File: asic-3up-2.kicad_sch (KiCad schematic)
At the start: 79 parts, among them J16 Conn_01x01, J17 Conn_01x01, J8 Conn_01x01, J9 Conn_01x01, U57 MCP1824T-1202E/OT, U58 MCP1824T-1202E/OT, U59 MCP1824T-1202E/OT, U60 MCP1824T-0802E, U61 MCP1824T-0802E, U62 MCP1824T-0802E, U63 BM1362AC_MODE1, U64 BM1362AC_MODE0, U65 BM1362AC_MODE1

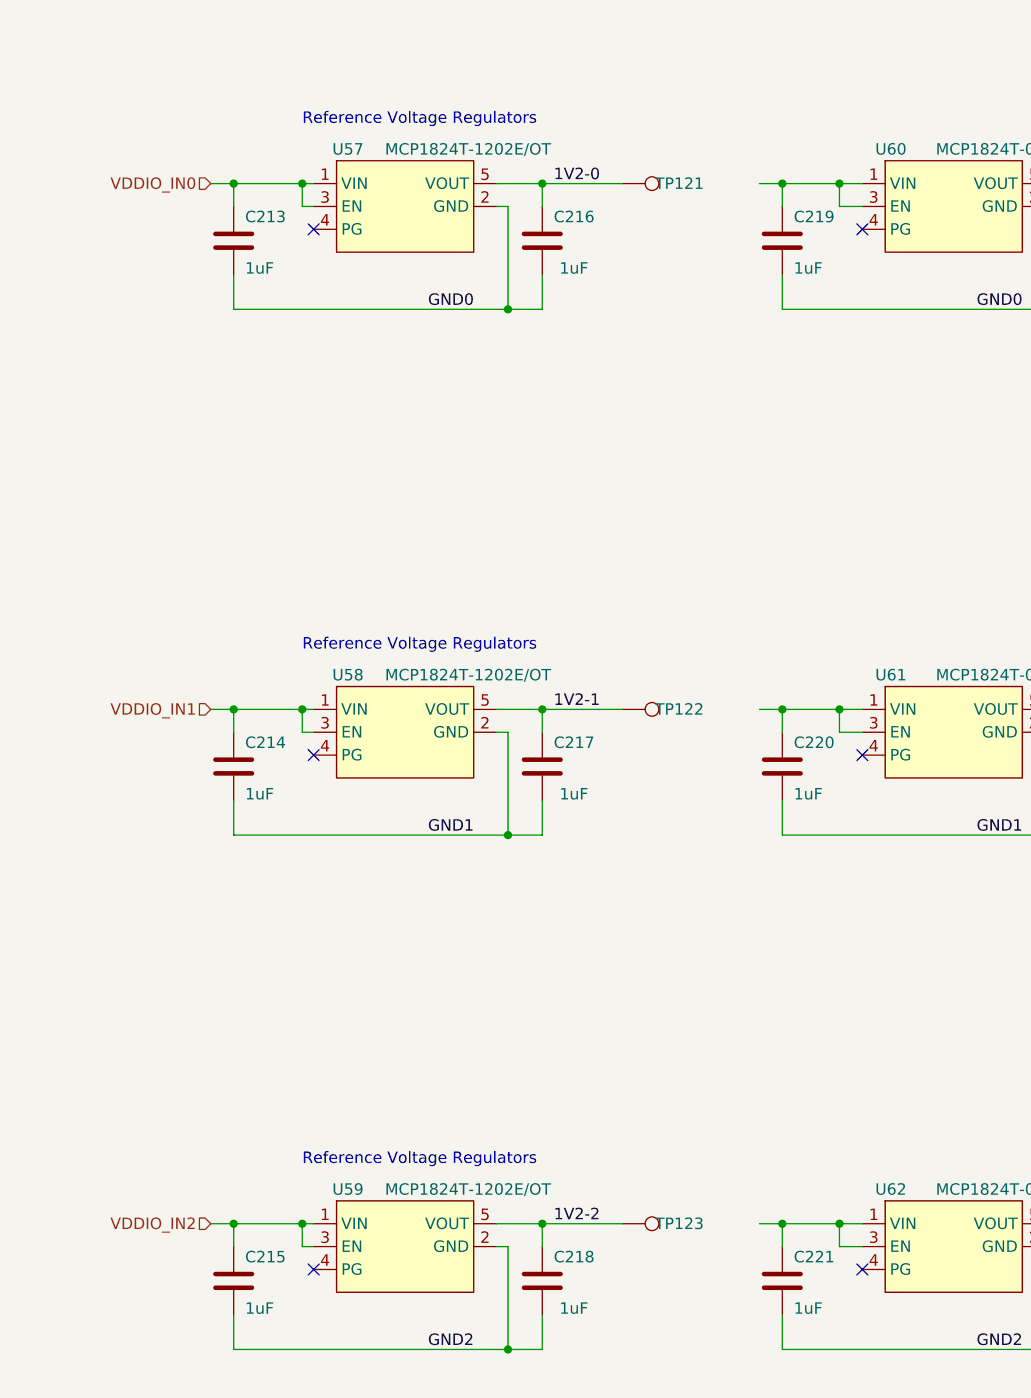
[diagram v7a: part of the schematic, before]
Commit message: added temp sensors. wired up (hopeful) vreg EN circuit. lots of LDO routing.
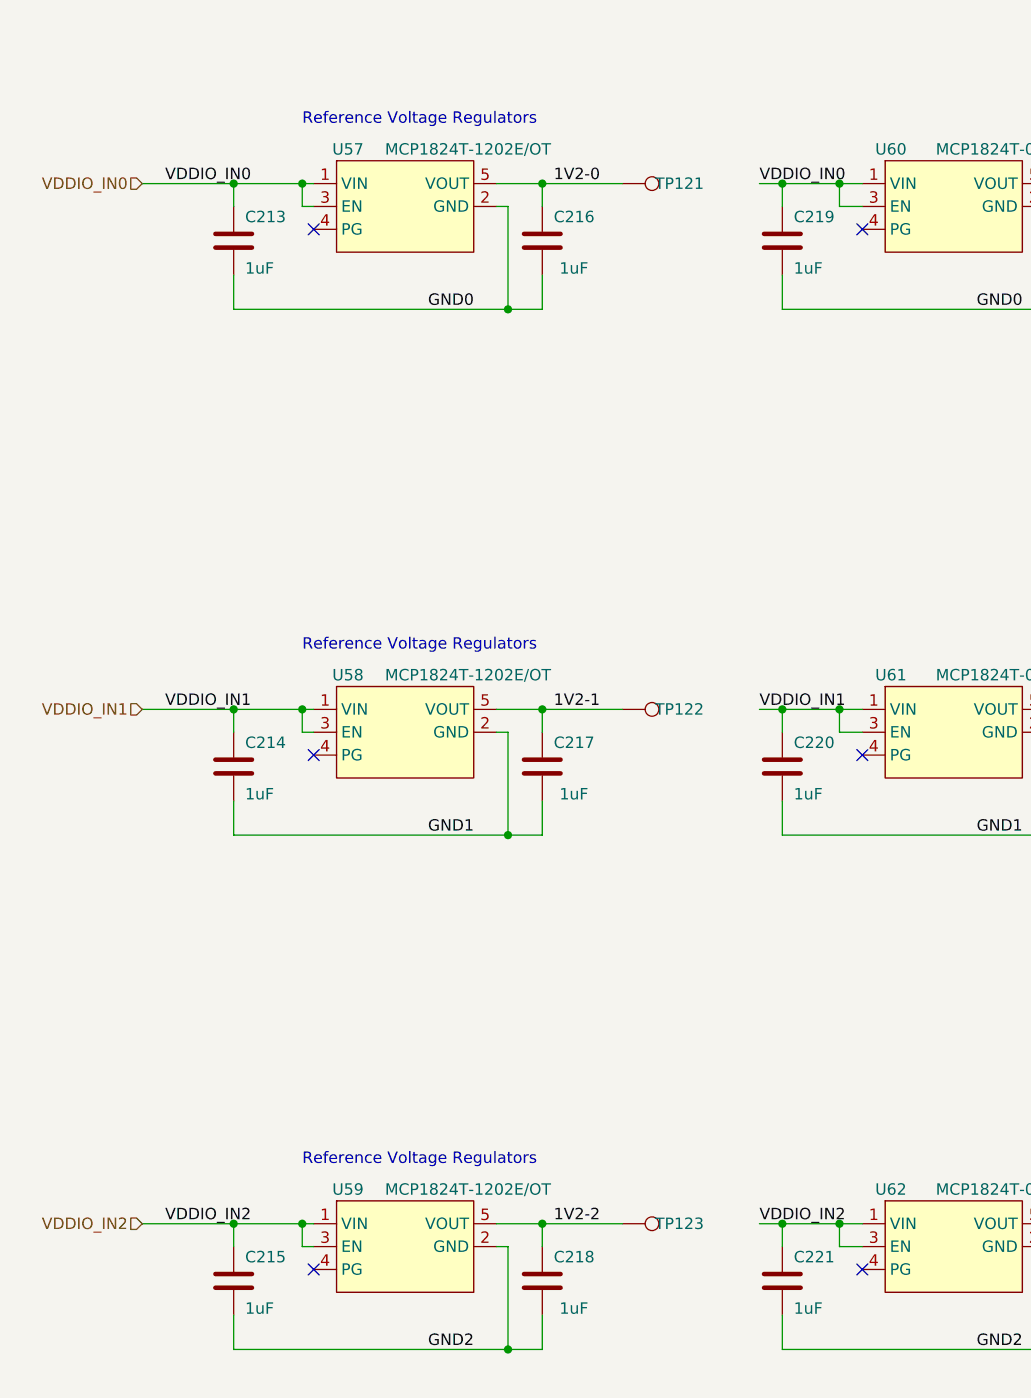
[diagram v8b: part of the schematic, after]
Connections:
- net VDDIO_IN0: now also C219.1, U60.1 (VIN), U60.3 (EN)
- net VDDIO_IN1: now also C220.1, U61.1 (VIN), U61.3 (EN)
- net VDDIO_IN2: now also C221.1, U62.1 (VIN), U62.3 (EN)
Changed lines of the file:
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@@
 	(wire
 		(pts
-			(xy 54.61 123.19) (xy 57.15 123.19)
+			(xy 46.99 123.19) (xy 57.15 123.19)
 		)
 		(stroke
@@
 	(wire
 		(pts
-			(xy 54.61 64.77) (xy 57.15 64.77)
+			(xy 46.99 64.77) (xy 57.15 64.77)
 		)
 		(stroke
@@
 	(wire
 		(pts
-			(xy 54.61 180.34) (xy 57.15 180.34)
+			(xy 46.99 180.34) (xy 57.15 180.34)
 		)
 		(stroke
@@
 		)
 	)
+	(label "VDDIO_IN0"
+		(at 49.53 64.77 0)
+		(fields_autoplaced yes)
+		(effects
+			(font
+				(size 1.27 1.27)
+			)
+			(justify left bottom)
+		)
+	)
 	(label "GND0"
 		(at 350.52 114.3 0)
@@
 		)
 	)
+	(label "VDDIO_IN2"
+		(at 49.53 180.34 0)
+		(fields_autoplaced yes)
+		(effects
+			(font
+				(size 1.27 1.27)
+			)
+			(justify left bottom)
+		)
+	)
 	(label "GND0"
 		(at 219.71 57.15 0)
@@
 		)
 	)
+	(label "VDDIO_IN0"
+		(at 115.57 64.77 0)
+		(fields_autoplaced yes)
+		(effects
+			(font
+				(size 1.27 1.27)
+			)
+			(justify left bottom)
+		)
+	)
 	(label "GND2"
 		(at 78.74 194.31 0)
@@
 		)
 	)
+	(label "VDDIO_IN1"
+		(at 115.57 123.19 0)
+		(fields_autoplaced yes)
+		(effects
+			(font
+				(size 1.27 1.27)
+			)
+			(justify left bottom)
+		)
+	)
 	(label "GND0"
 		(at 306.07 90.17 0)
@@
 		)
 	)
+	(label "VDDIO_IN2"
+		(at 115.57 180.34 0)
+		(fields_autoplaced yes)
+		(effects
+			(font
+				(size 1.27 1.27)
+			)
+			(justify left bottom)
+		)
+	)
 	(label "0V8-2"
 		(at 219.71 194.31 0)
@@
 			)
 			(justify right bottom)
+		)
+	)
+	(label "VDDIO_IN1"
+		(at 49.53 123.19 0)
+		(fields_autoplaced yes)
+		(effects
+			(font
+				(size 1.27 1.27)
+			)
+			(justify left bottom)
 		)
 	)
@@
 	(hierarchical_label "VDDIO_IN0"
 		(shape input)
-		(at 54.61 64.77 180)
+		(at 46.99 64.77 180)
 		(fields_autoplaced yes)
 		(effects
@@
 	(hierarchical_label "VDDIO_IN1"
 		(shape input)
-		(at 54.61 123.19 180)
+		(at 46.99 123.19 180)
 		(fields_autoplaced yes)
 		(effects
@@
 	(hierarchical_label "VDDIO_IN2"
 		(shape input)
-		(at 54.61 180.34 180)
-		(fields_autoplaced yes)
-		(effects
+		(at 46.99 180.34 180)
+		(fields_autoplaced yes)
+		(effects
